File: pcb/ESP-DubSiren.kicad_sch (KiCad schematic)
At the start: 12 parts, among them SW1 TRIGGER, SW2 MOD DOWN, SW3 MOD UP, SW4 ECHO CUT, U1 ESP32-S3-DevKitC-1 N16R8, U2 PCM5102A BREAKOUT PROVISIONAL

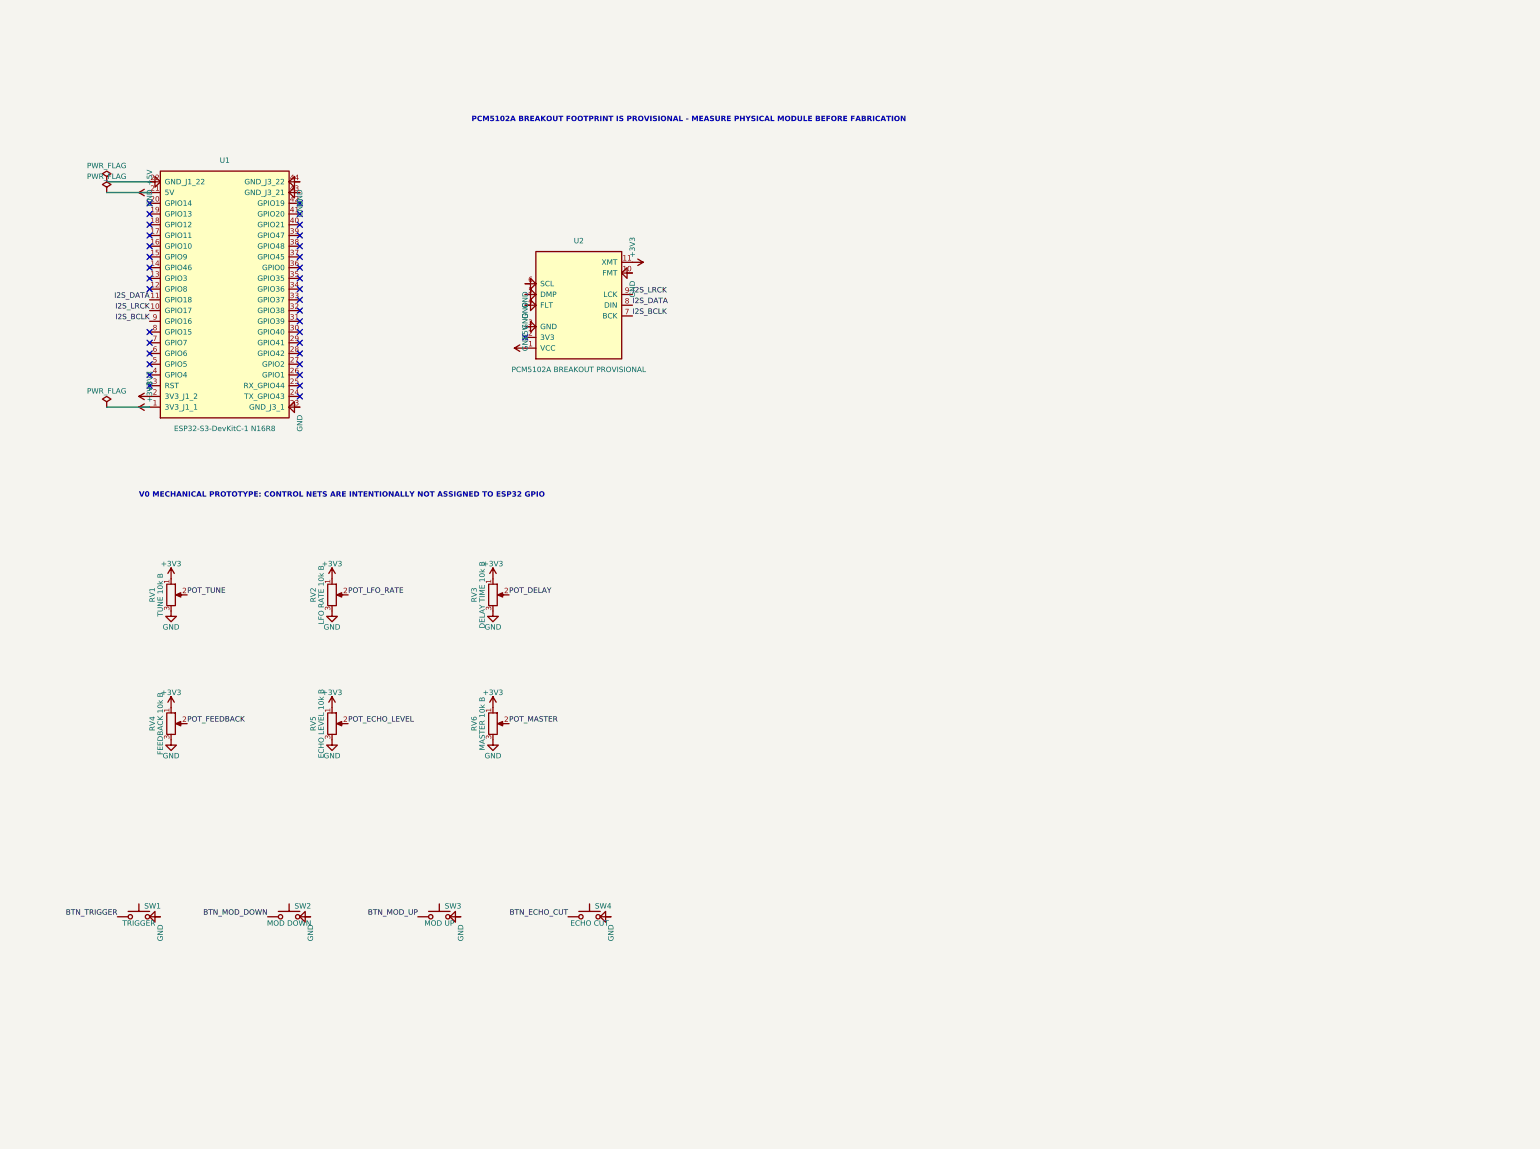
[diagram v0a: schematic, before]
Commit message: pcb: add ESP32-S3 mainboard V1 preproduction design
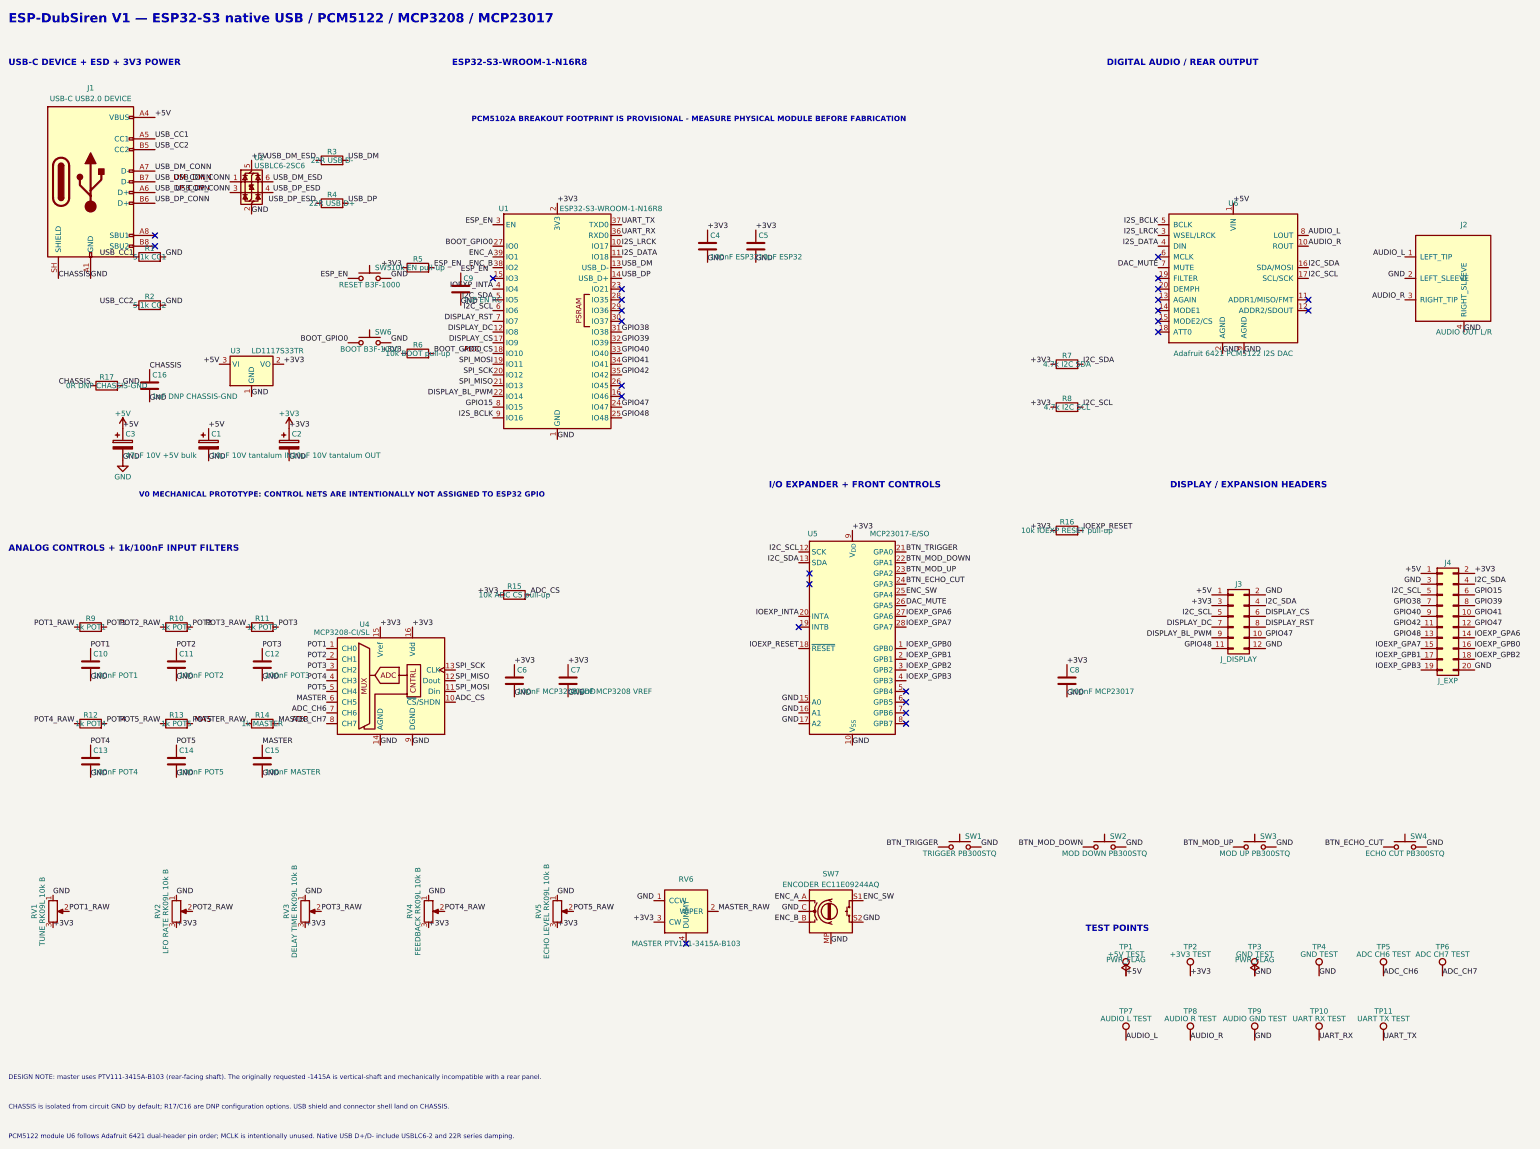
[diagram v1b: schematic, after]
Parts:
- removed RV6: MASTER 10k B, Potentiometer_THT:Potentiometer_Alps_RK09L_Single_Vertical, symbol Device:R_Potentiometer
- removed U1: ESP32-S3-DevKitC-1 N16R8, ESP-DubSiren:ESP32-S3-DevKitC-1_N16R8, symbol ESP-DubSiren:ESP32-S3-DevKitC-1_N16R8
- removed U2: PCM5102A BREAKOUT PROVISIONAL, ESP-DubSiren:PCM5102A_BREAKOUT_PROVISIONAL, symbol ESP-DubSiren:PCM5102A_BREAKOUT_PROVISIONAL
- added C1: 10uF 10V tantalum IN, Capacitor_Tantalum_SMD:CP_EIA-3528-21_Kemet-B, symbol Device:C_Polarized
- added C10: 100nF POT1, Capacitor_SMD:C_0603_1608Metric, symbol Device:C
- added C11: 100nF POT2, Capacitor_SMD:C_0603_1608Metric, symbol Device:C
- added C12: 100nF POT3, Capacitor_SMD:C_0603_1608Metric, symbol Device:C
- added C13: 100nF POT4, Capacitor_SMD:C_0603_1608Metric, symbol Device:C
- added C14: 100nF POT5, Capacitor_SMD:C_0603_1608Metric, symbol Device:C
- added C15: 100nF MASTER, Capacitor_SMD:C_0603_1608Metric, symbol Device:C
- added C16: 1nF DNP CHASSIS-GND, Capacitor_SMD:C_0603_1608Metric, symbol Device:C
- added C2: 10uF 10V tantalum OUT, Capacitor_Tantalum_SMD:CP_EIA-3528-21_Kemet-B, symbol Device:C_Polarized
- added C3: 47uF 10V +5V bulk, Capacitor_SMD:CP_Elec_6.3x5.3, symbol Device:C_Polarized
- added C4: 100nF ESP32, Capacitor_SMD:C_0603_1608Metric, symbol Device:C
- added C5: 10uF ESP32, Capacitor_SMD:C_1206_3216Metric, symbol Device:C
- added C6: 100nF MCP3208 VDD, Capacitor_SMD:C_0603_1608Metric, symbol Device:C
- added C7: 100nF MCP3208 VREF, Capacitor_SMD:C_0603_1608Metric, symbol Device:C
- added C8: 100nF MCP23017, Capacitor_SMD:C_0603_1608Metric, symbol Device:C
- added C9: 1uF EN RC, Capacitor_SMD:C_0805_2012Metric, symbol Device:C
- added J1: USB-C USB2.0 DEVICE, Connector_USB:USB_C_Receptacle_GCT_USB4085, symbol Connector:USB_C_Receptacle_USB2.0_16P
- added J2: AUDIO OUT L/R, ESP-DubSiren:Switchcraft_PJRAS2X1S02X, symbol ESP-DubSiren:PJRAS2X1S02X
- added J3: J_DISPLAY, Connector_PinHeader_2.54mm:PinHeader_2x06_P2.54mm_Vertical, symbol Connector_Generic:Conn_02x06_Odd_Even
- added J4: J_EXP, Connector_PinHeader_2.54mm:PinHeader_2x10_P2.54mm_Vertical, symbol Connector_Generic:Conn_02x10_Odd_Even
- added R1: 5.1k CC1, Resistor_SMD:R_0603_1608Metric, symbol Device:R
- added R10: 1k POT2, Resistor_SMD:R_0603_1608Metric, symbol Device:R
- added R11: 1k POT3, Resistor_SMD:R_0603_1608Metric, symbol Device:R
- added R12: 1k POT4, Resistor_SMD:R_0603_1608Metric, symbol Device:R
- added R13: 1k POT5, Resistor_SMD:R_0603_1608Metric, symbol Device:R
- added R14: 1k MASTER, Resistor_SMD:R_0603_1608Metric, symbol Device:R
- added R15: 10k ADC CS pull-up, Resistor_SMD:R_0603_1608Metric, symbol Device:R
- added R16: 10k IOEXP RESET pull-up, Resistor_SMD:R_0603_1608Metric, symbol Device:R
- added R17: 0R DNP CHASSIS-GND, Resistor_SMD:R_0603_1608Metric, symbol Device:R
- added R2: 5.1k CC2, Resistor_SMD:R_0603_1608Metric, symbol Device:R
- added R3: 22R USB D-, Resistor_SMD:R_0603_1608Metric, symbol Device:R
- added R4: 22R USB D+, Resistor_SMD:R_0603_1608Metric, symbol Device:R
- added R5: 10k EN pull-up, Resistor_SMD:R_0603_1608Metric, symbol Device:R
- added R6: 10k BOOT pull-up, Resistor_SMD:R_0603_1608Metric, symbol Device:R
- added R7: 4.7k I2C SDA, Resistor_SMD:R_0603_1608Metric, symbol Device:R
- added R8: 4.7k I2C SCL, Resistor_SMD:R_0603_1608Metric, symbol Device:R
- added R9: 1k POT1, Resistor_SMD:R_0603_1608Metric, symbol Device:R
- added RV6: MASTER PTV111-3415A-B103, ESP-DubSiren:Bourns_PTV111-3415A-B103, symbol ESP-DubSiren:PTV111-3415A-B103
- added SW5: RESET B3F-1000, Button_Switch_THT:SW_PUSH_6mm_H4.3mm, symbol Switch:SW_Push
- added SW6: BOOT B3F-1000, Button_Switch_THT:SW_PUSH_6mm_H4.3mm, symbol Switch:SW_Push
- added SW7: ENCODER EC11E09244AQ, Rotary_Encoder:RotaryEncoder_Alps_EC11E-Switch_Vertical_H20mm, symbol Device:RotaryEncoder_Switch_MP
- added TP1: +5V TEST, TestPoint:TestPoint_Pad_D1.0mm, symbol Connector:TestPoint
- added TP10: UART RX TEST, TestPoint:TestPoint_Pad_D1.0mm, symbol Connector:TestPoint
- added TP11: UART TX TEST, TestPoint:TestPoint_Pad_D1.0mm, symbol Connector:TestPoint
- added TP2: +3V3 TEST, TestPoint:TestPoint_Pad_D1.0mm, symbol Connector:TestPoint
- added TP3, TP4: GND TEST, TestPoint:TestPoint_Pad_D1.0mm, symbol Connector:TestPoint
- added TP5: ADC CH6 TEST, TestPoint:TestPoint_Pad_D1.0mm, symbol Connector:TestPoint
- added TP6: ADC CH7 TEST, TestPoint:TestPoint_Pad_D1.0mm, symbol Connector:TestPoint
- added TP7: AUDIO L TEST, TestPoint:TestPoint_Pad_D1.0mm, symbol Connector:TestPoint
- added TP8: AUDIO R TEST, TestPoint:TestPoint_Pad_D1.0mm, symbol Connector:TestPoint
- added TP9: AUDIO GND TEST, TestPoint:TestPoint_Pad_D1.0mm, symbol Connector:TestPoint
- added U1: ESP32-S3-WROOM-1-N16R8, RF_Module:ESP32-S3-WROOM-1, symbol RF_Module:ESP32-S3-WROOM-1
- added U2: USBLC6-2SC6, Package_TO_SOT_SMD:SOT-23-6, symbol Power_Protection:USBLC6-2SC6
- added U3: LD1117S33TR, Package_TO_SOT_SMD:SOT-223-3_TabPin2, symbol Regulator_Linear:LD1117S33TR_SOT223
- added U4: MCP3208-CI/SL, Package_SO:SOIC-16_3.9x9.9mm_P1.27mm, symbol Analog_ADC:MCP3208
- added U5: MCP23017-E/SO, Package_SO:SOIC-28W_7.5x17.9mm_P1.27mm, symbol Interface_Expansion:MCP23017x-x-SO
- added U6: Adafruit 6421 PCM5122 I2S DAC, ESP-DubSiren:Adafruit_PCM5122_6421, symbol ESP-DubSiren:Adafruit_PCM5122_6421
- RV1: value TUNE 10k B -> TUNE RK09L 10k B
- RV2: value LFO RATE 10k B -> LFO RATE RK09L 10k B
- RV3: value DELAY TIME 10k B -> DELAY TIME RK09L 10k B
- RV4: value FEEDBACK 10k B -> FEEDBACK RK09L 10k B
- RV5: value ECHO LEVEL 10k B -> ECHO LEVEL RK09L 10k B
- SW1: value TRIGGER -> TRIGGER PB300STQ; MPN (none) -> PB300STQ; Manufacturer (none) -> E-Switch
- SW2: value MOD DOWN -> MOD DOWN PB300STQ; MPN (none) -> PB300STQ; Manufacturer (none) -> E-Switch
- SW3: value MOD UP -> MOD UP PB300STQ; MPN (none) -> PB300STQ; Manufacturer (none) -> E-Switch
- SW4: value ECHO CUT -> ECHO CUT PB300STQ; MPN (none) -> PB300STQ; Manufacturer (none) -> E-Switch
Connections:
- net +3V3: now also RV1.3, RV2.3, RV3.3, RV4.3, RV5.3, C2.1, C4.1, C5.1, C6.1, C7.1, C8.1, J3.3 (Pin_3), J4.2 (Pin_2), R15.1, R16.1, R5.1, R6.1, R7.1, R8.1, RV6.3 (CW), TP2.1, U1.2 (3V3), U3.2 (VO), U4.15 (Vref), U4.16 (Vdd), U5.9 (V_{DD}); no longer RV1.1, RV2.1, RV3.1, RV4.1, RV5.1
- net +5V: now also C1.1, C3.1, J1.A4 (VBUS), J1.A9 (VBUS), J1.B4 (VBUS), J1.B9 (VBUS), J3.1 (Pin_1), J4.1 (Pin_1), TP1.1, U2.5 (VBUS), U3.3 (VI), U6.1 (VIN)
- net BTN_ECHO_CUT: now also U5.24 (GPA3)
- net BTN_MOD_DOWN: now also U5.22 (GPA1)
- net BTN_MOD_UP: now also U5.23 (GPA2)
- net BTN_TRIGGER: now also U5.21 (GPA0)
- net GND: now also RV1.1, RV2.1, RV3.1, RV4.1, RV5.1, C1.2, C10.2, C11.2, C12.2, C13.2, C14.2, C15.2, C16.2, C2.2, C3.2, C4.2, C5.2, C6.2, C7.2, C8.2, C9.2, J1.A1 (GND), J1.A12 (GND), J1.B1 (GND), J1.B12 (GND), J2.2 (LEFT_SLEEVE), J2.4 (RIGHT_SLEEVE), J3.12 (Pin_12), J3.2 (Pin_2), J4.20 (Pin_20), J4.3 (Pin_3), R1.2, R17.2, R2.2, RV6.1 (CCW), SW5.2, SW6.2, SW7.C, SW7.MP, SW7.S2, TP3.1, TP4.1, TP9.1, U1.1 (GND), U1.40 (GND), U1.41 (GND), U2.2 (GND), U3.1 (GND), U4.14 (AGND), U4.9 (DGND), U5.10 (V_{SS}), U5.15 (A0), U5.16 (A1), U5.17 (A2), U6.2 (AGND), U6.9 (AGND); no longer RV1.3, RV2.3, RV3.3, RV4.3, RV5.3
- net I2S_BCLK: now also U1.9 (IO16), U6.5 (BCLK)
- net I2S_DATA: now also U1.11 (IO18), U6.4 (DIN)
- net I2S_LRCK: now also U1.10 (IO17), U6.3 (WSEL/LRCK)
- net POT_DELAY renamed POT3_RAW
- net POT3_RAW: now also R11.1
- net POT_ECHO_LEVEL renamed POT5_RAW
- net POT5_RAW: now also R13.1
- net POT_FEEDBACK renamed POT4_RAW
- net POT4_RAW: now also R12.1
- net POT_LFO_RATE renamed POT2_RAW
- net POT2_RAW: now also R10.1
- net POT_TUNE renamed POT1_RAW
- net POT1_RAW: now also R9.1
- new net ADC_CH6: TP5.1, U4.7 (CH6)
- new net ADC_CH7: TP6.1, U4.8 (CH7)
- new net ADC_CS: R15.2, U1.18 (IO10), U4.10 (~{CS}/SHDN)
- new net AUDIO_L: J2.1 (LEFT_TIP), TP7.1, U6.8 (LOUT)
- new net AUDIO_R: J2.3 (RIGHT_TIP), TP8.1, U6.10 (ROUT)
- new net BOOT_GPIO0: R6.2, SW6.1, U1.27 (IO0)
- new net CHASSIS: C16.1, J1.SH (SHIELD), R17.1
- new net DAC_MUTE: U5.26 (GPA5), U6.7 (MUTE)
- new net DISPLAY_BL_PWM: J3.9 (Pin_9), U1.22 (IO14)
- new net DISPLAY_CS: J3.6 (Pin_6), U1.17 (IO9)
- new net DISPLAY_DC: J3.7 (Pin_7), U1.12 (IO8)
- new net DISPLAY_RST: J3.8 (Pin_8), U1.7 (IO7)
- new net ENC_A: SW7.A, U1.39 (IO1)
- new net ENC_B: SW7.B, U1.38 (IO2)
- new net ENC_SW: SW7.S1, U5.25 (GPA4)
- new net ESP_EN: C9.1, R5.2, SW5.1, U1.3 (EN)
- new net GPIO15: J4.6 (Pin_6), U1.8 (IO15)
- new net GPIO38: J4.7 (Pin_7), U1.31 (IO38)
- new net GPIO39: J4.8 (Pin_8), U1.32 (IO39)
- new net GPIO40: J4.9 (Pin_9), U1.33 (IO40)
- new net GPIO41: J4.10 (Pin_10), U1.34 (IO41)
- new net GPIO42: J4.11 (Pin_11), U1.35 (IO42)
- new net GPIO47: J3.10 (Pin_10), J4.12 (Pin_12), U1.24 (IO47)
- new net GPIO48: J3.11 (Pin_11), J4.13 (Pin_13), U1.25 (IO48)
- new net I2C_SCL: J3.5 (Pin_5), J4.5 (Pin_5), R8.2, U1.6 (IO6), U5.12 (SCK), U6.17 (SCL/SCK)
- new net I2C_SDA: J3.4 (Pin_4), J4.4 (Pin_4), R7.2, U1.5 (IO5), U5.13 (SDA), U6.16 (SDA/MOSI)
- new net IOEXP_GPA6: J4.14 (Pin_14), U5.27 (GPA6)
- new net IOEXP_GPA7: J4.15 (Pin_15), U5.28 (GPA7)
- new net IOEXP_GPB0: J4.16 (Pin_16), U5.1 (GPB0)
- new net IOEXP_GPB1: J4.17 (Pin_17), U5.2 (GPB1)
- new net IOEXP_GPB2: J4.18 (Pin_18), U5.3 (GPB2)
- new net IOEXP_GPB3: J4.19 (Pin_19), U5.4 (GPB3)
- new net IOEXP_INTA: U1.4 (IO4), U5.20 (INTA)
- new net IOEXP_RESET: R16.2, U5.18 (~{RESET})
- new net MASTER: C15.1, R14.2, U4.6 (CH5)
- new net MASTER_RAW: R14.1, RV6.2 (WIPER)
- new net POT1: C10.1, R9.2, U4.1 (CH0)
- new net POT2: C11.1, R10.2, U4.2 (CH1)
- new net POT3: C12.1, R11.2, U4.3 (CH2)
- new net POT4: C13.1, R12.2, U4.4 (CH3)
- new net POT5: C14.1, R13.2, U4.5 (CH4)
- new net SPI_MISO: U1.21 (IO13), U4.12 (Dout)
- new net SPI_MOSI: U1.19 (IO11), U4.11 (Din)
- new net SPI_SCK: U1.20 (IO12), U4.13 (CLK)
- new net UART_RX: TP10.1, U1.36 (RXD0)
- new net UART_TX: TP11.1, U1.37 (TXD0)
- new net USB_CC1: J1.A5 (CC1), R1.1
- new net USB_CC2: J1.B5 (CC2), R2.1
- new net USB_DM: R3.2, U1.13 (USB_D-)
- new net USB_DM_CONN: J1.A7 (D-), J1.B7 (D-), U2.1 (I/O1)
- new net USB_DM_ESD: R3.1, U2.6 (I/O1)
- new net USB_DP: R4.2, U1.14 (USB_D+)
- new net USB_DP_CONN: J1.A6 (D+), J1.B6 (D+), U2.3 (I/O2)
- new net USB_DP_ESD: R4.1, U2.4 (I/O2)
- no-connect marks 35 -> 26
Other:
- note added: "ANALOG CONTROLS + 1k/100nF INPUT FILTERS"
- note added: "CHASSIS is isolated from circuit GND by default; R17/C16 are DNP configuration options. USB shield and connector shell land on CHASSIS."
- note added: "DESIGN NOTE: master uses PTV111-3415A-B103 (rear-facing shaft). The originally requested -1415A is vertical-shaft and mechanically incompatible with a rear panel."
- note added: "DIGITAL AUDIO / REAR OUTPUT"
- note added: "DISPLAY / EXPANSION HEADERS"
- note added: "ESP-DubSiren V1 — ESP32-S3 native USB / PCM5122 / MCP3208 / MCP23017"
- note added: "ESP32-S3-WROOM-1-N16R8"
- note added: "I/O EXPANDER + FRONT CONTROLS"
- note added: "PCM5122 module U6 follows Adafruit 6421 dual-header pin order; MCLK is intentionally unused. Native USB D+/D- include USBLC6-2 and 22R series damping."
- note added: "TEST POINTS"
- note added: "USB-C DEVICE + ESD + 3V3 POWER"
